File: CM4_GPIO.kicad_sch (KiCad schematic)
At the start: 17 parts, among them J10 Conn_02x03_Odd_Even, J8 Conn_01x02, J9 THD-20-R, U6 74LVC1G07SE-7, U7 MagJack-A70-112-331N126

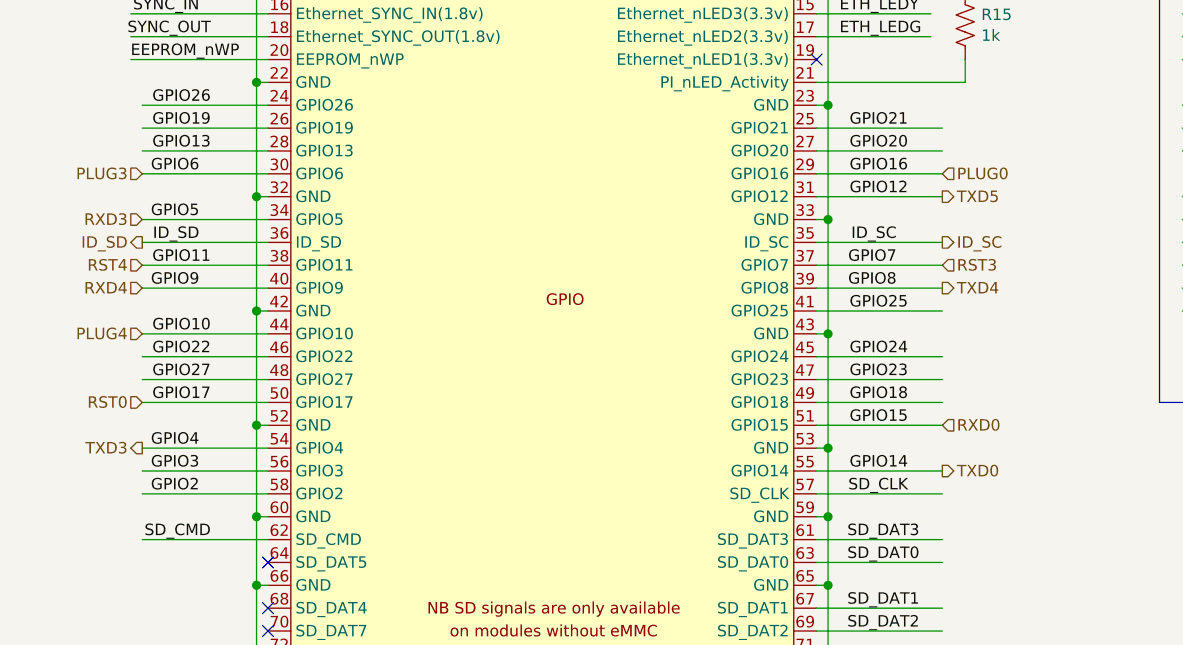
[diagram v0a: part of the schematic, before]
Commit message: added more USB ports.. placing
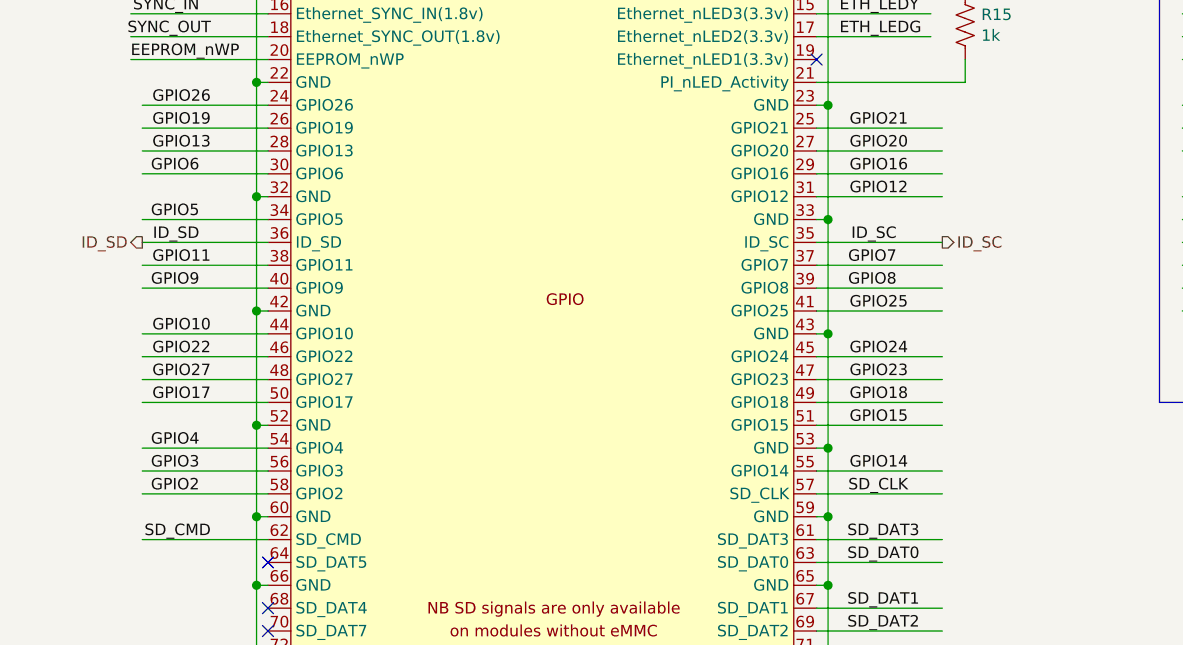
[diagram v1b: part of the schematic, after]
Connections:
- net PLUG0 renamed GPIO16
- net PLUG3 renamed GPIO6
- net PLUG4 renamed GPIO10
- net RST0 renamed GPIO17
- net RST3 renamed GPIO7
- net RST4 renamed GPIO11
- net RXD0 renamed GPIO15
- net RXD3 renamed GPIO5
- net RXD4 renamed GPIO9
- net TXD0 renamed GPIO14
- net TXD3 renamed GPIO4
- net TXD4 renamed GPIO8
- net TXD5 renamed GPIO12
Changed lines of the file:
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@@
-		)
-	)
-	(hierarchical_label "RXD4"
-		(shape input)
-		(at 25.4 67.31 180)
-		(fields_autoplaced yes)
-		(effects
-			(font
-				(size 1.27 1.27)
-			)
-			(justify right)
-		)
-	)
-	(hierarchical_label "TXD5"
-		(shape output)
-		(at 114.3 57.15 0)
-		(fields_autoplaced yes)
-		(effects
-			(font
-				(size 1.27 1.27)
-			)
-			(justify left)
-		)
-	)
-	(hierarchical_label "RST0"
-		(shape input)
-		(at 25.4 80.01 180)
-		(fields_autoplaced yes)
-		(effects
-			(font
-				(size 1.27 1.27)
-			)
-			(justify right)
-		)
-	)
-	(hierarchical_label "TXD0"
-		(shape output)
-		(at 114.3 87.63 0)
-		(fields_autoplaced yes)
-		(effects
-			(font
-				(size 1.27 1.27)
-			)
-			(justify left)
-		)
-	)
-	(hierarchical_label "PLUG3"
-		(shape input)
-		(at 25.4 54.61 180)
-		(fields_autoplaced yes)
-		(effects
-			(font
-				(size 1.27 1.27)
-			)
-			(justify right)
-		)
-	)
-	(hierarchical_label "RXD3"
-		(shape input)
-		(at 25.4 59.69 180)
-		(fields_autoplaced yes)
-		(effects
-			(font
-				(size 1.27 1.27)
-			)
-			(justify right)
-		)
-	)
-	(hierarchical_label "TXD4"
-		(shape output)
-		(at 114.3 67.31 0)
-		(fields_autoplaced yes)
-		(effects
-			(font
-				(size 1.27 1.27)
-			)
-			(justify left)
-		)
-	)
-	(hierarchical_label "RST3"
-		(shape input)
-		(at 114.3 64.77 0)
-		(fields_autoplaced yes)
-		(effects
-			(font
-				(size 1.27 1.27)
-			)
-			(justify left)
-		)
-	)
-	(hierarchical_label "PLUG4"
-		(shape input)
-		(at 25.4 72.39 180)
-		(fields_autoplaced yes)
-		(effects
-			(font
-				(size 1.27 1.27)
-			)
-			(justify right)
 		)
 	)
@@
 		)
 	)
-	(hierarchical_label "RST4"
-		(shape input)
-		(at 25.4 64.77 180)
-		(fields_autoplaced yes)
-		(effects
-			(font
-				(size 1.27 1.27)
-			)
-			(justify right)
-		)
-	)
 	(hierarchical_label "nEXTRST"
 		(shape output)
@@
 		)
 	)
-	(hierarchical_label "RXD0"
-		(shape input)
-		(at 114.3 82.55 0)
-		(fields_autoplaced yes)
-		(effects
-			(font
-				(size 1.27 1.27)
-			)
-			(justify left)
-		)
-	)
-	(hierarchical_label "PLUG0"
-		(shape input)
-		(at 114.3 54.61 0)
-		(fields_autoplaced yes)
-		(effects
-			(font
-				(size 1.27 1.27)
-			)
-			(justify left)
-		)
-	)
 	(hierarchical_label "3V3"
 		(shape output)
@@
 		(fields_autoplaced yes)
 		(effects
-			(font
-				(size 1.27 1.27)
-			)
-			(justify right)
-		)
-	)
-	(hierarchical_label "TXD3"
-		(shape output)
-		(at 25.4 85.09 180)
-		(fields_autoplaced yes)
-		(effects
